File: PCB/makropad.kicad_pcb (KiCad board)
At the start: 2 copper layers, 82 x 85 mm, 55 parts, among them J1 OLED_DISPLAY, J2 Conn_01x04, SW1 SW_Push_45deg, SW10 SW_Push_45deg, SW11 RotaryEncoder_Switch, SW12 RotaryEncoder_Switch, SW2 SW_Push_45deg, SW3 SW_Push_45deg, SW4 SW_Push_45deg, SW5 SW_Push_45deg, SW6 SW_Push_45deg, SW7 SW_Push_45deg, SW8 SW_Push_45deg, SW9 SW_Push_45deg, U1 PCF8574A, U2 MOUDLE-SEEEDUINO-XIAO

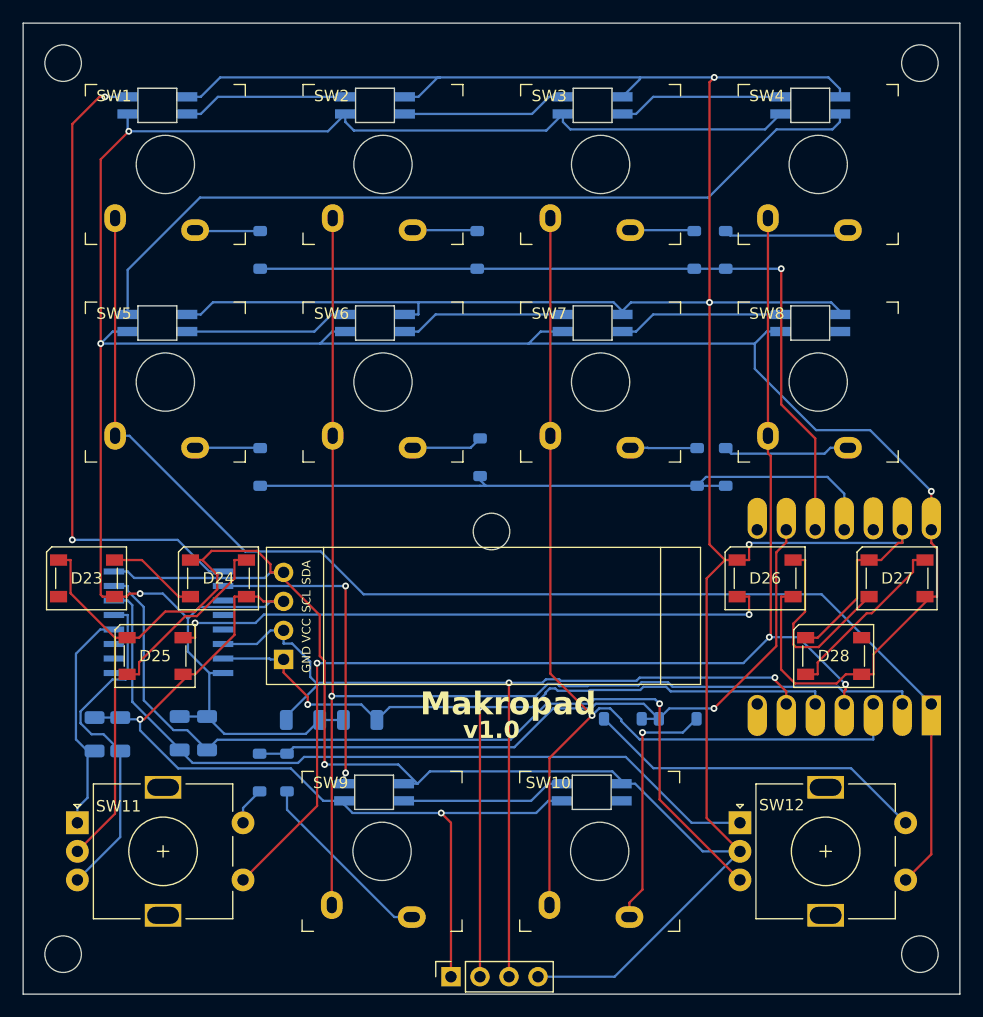
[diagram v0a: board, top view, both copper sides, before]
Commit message: feat: pull up i2c lines to 3.3v and remove encoder pull ups
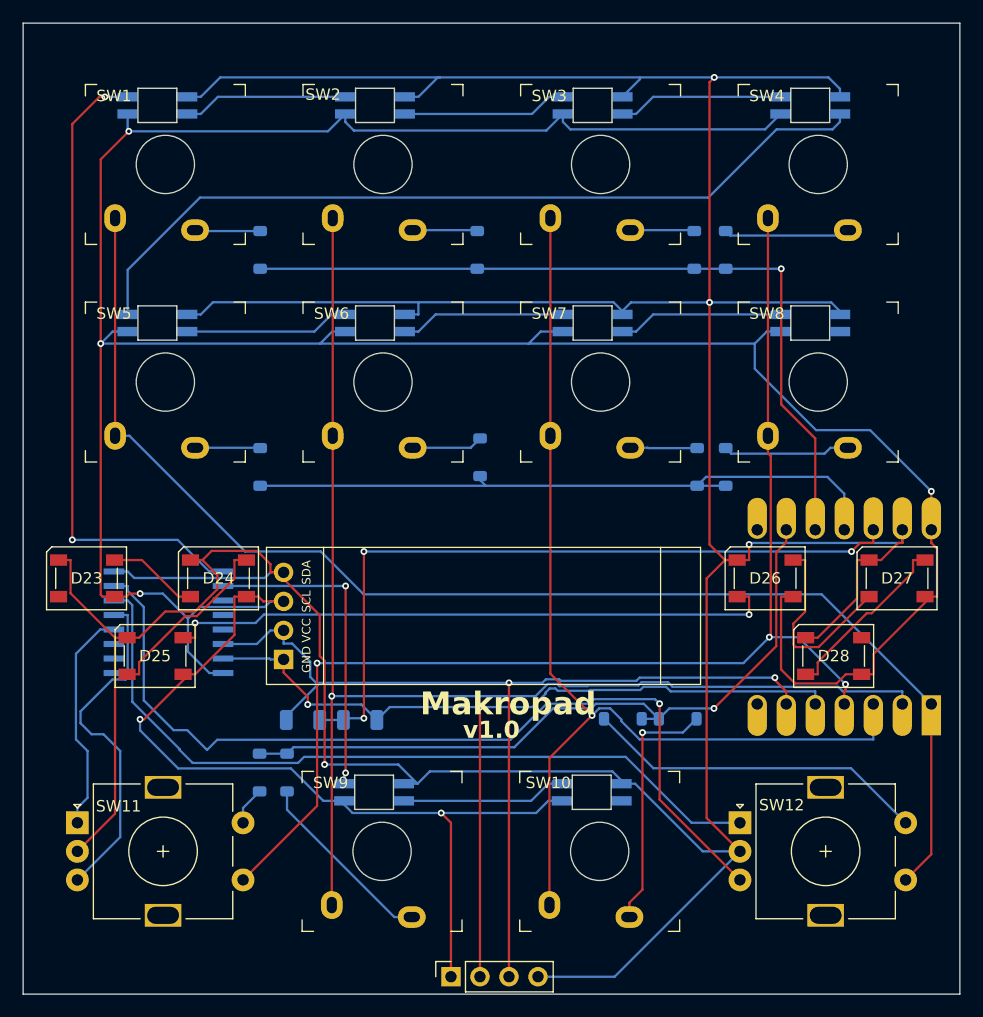
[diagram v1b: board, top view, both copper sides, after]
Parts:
- removed MH1, MH2, MH3, MH4 (x2): MountingHole_3.2mm_M3, MountingHole:MountingHole_3.2mm_M3
- removed R3, R4, R5, R6: 10k, Resistor_SMD:R_1206_3216Metric
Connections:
- R1 pad 2: VCC -> +3.3V
- R2 pad 2: VCC -> +3.3V
- U2 pad 12: unconnected-(U2-3V3-Pad12) -> +3.3V
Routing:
- net +3.3V: track 0.00 -> 64.6 mm, vias 0 -> 3
- net VCC: track 354.4 -> 331.0 mm
- net ENC_1_A: track 20.4 -> 19.8 mm

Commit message: fuck
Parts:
- D13, D14, D15, D16, D17, D18, D19, D20, D21, D22: footprint Components:SK6812MINI-E -> Components:LED_SK6812MINI
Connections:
- U1 pad 11: unconnected-(U1-P6-Pad11) -> STATUS_LED
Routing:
- net VCC: track 331.0 -> 366.6 mm, vias 6 -> 7
- net STATUS_LED: track 0.00 -> 25.4 mm, vias 0 -> 1
- net Net-(D16-DOUT): track 72.3 -> 80.3 mm
- net COL2: track 92.4 -> 99.8 mm
- net COL1: track 112.2 -> 119.6 mm
- net RGB: track 56.6 -> 50.8 mm
- net ROW1: track 58.8 -> 55.3 mm
- net RGB2: track 28.1 -> 31.2 mm
- net GND: track 380.8 -> 379.6 mm
- net Net-(D10-A): track 16.4 -> 17.4 mm
- net COL0: track 116.6 -> 117.2 mm

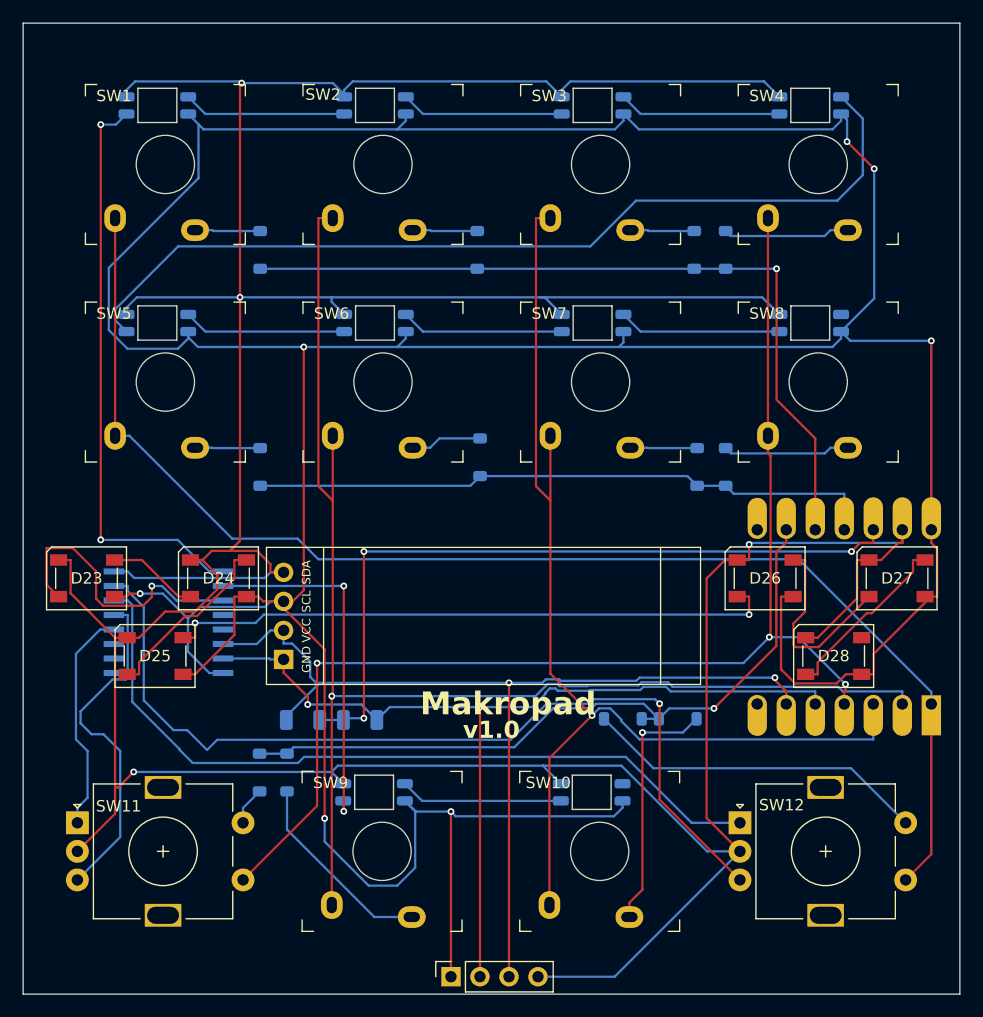
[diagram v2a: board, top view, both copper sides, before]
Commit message: finally finish up pcb and fix led wiring
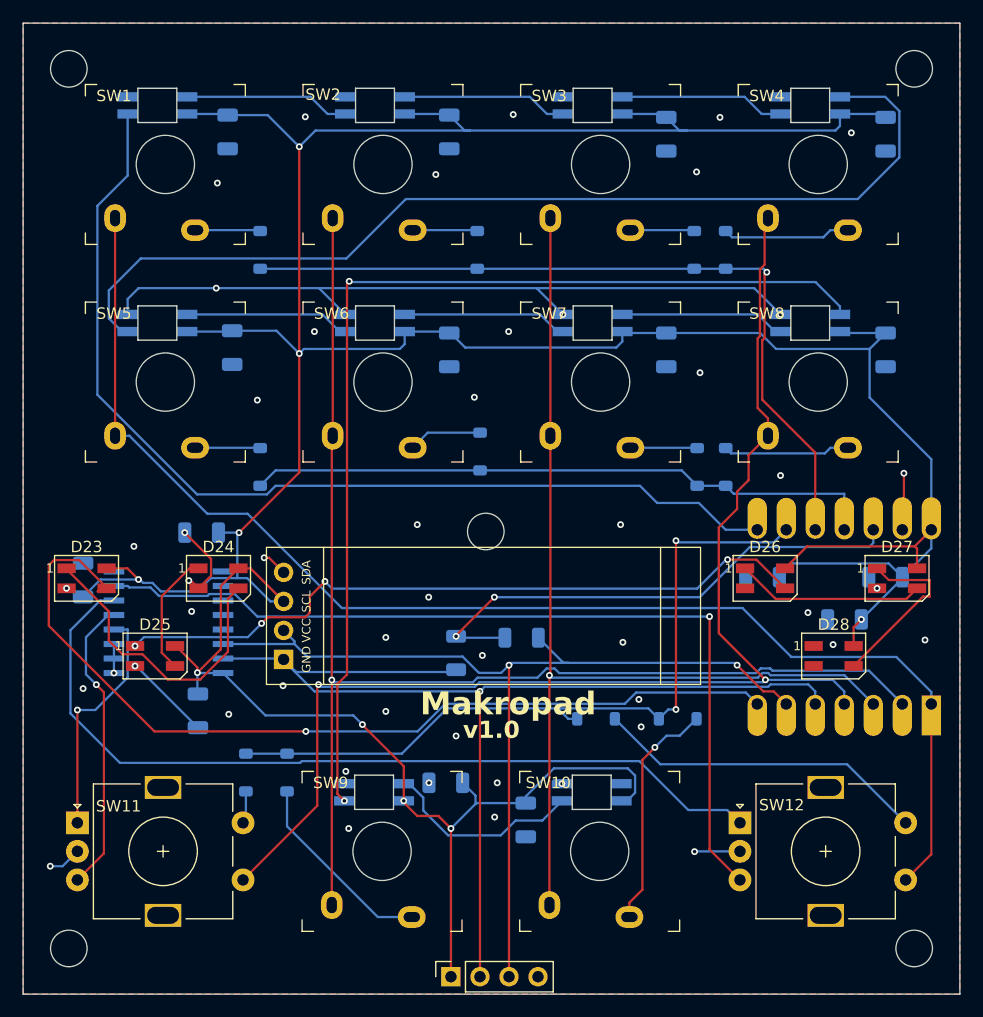
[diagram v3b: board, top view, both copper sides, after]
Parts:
- added C1: 0.1uF, Capacitor_SMD:C_1206_3216Metric, B.Cu at (129.4, 52.5)
- added C10: 0.1uF, Capacitor_SMD:C_1206_3216Metric, B.Cu at (155.5, 112.8)
- added C11: 0.1uF, Capacitor_SMD:C_1206_3216Metric, B.Cu at (116.8, 91.8)
- added C12: 0.1uF, Capacitor_SMD:C_1206_3216Metric, B.Cu at (127.1, 87.6)
- added C13: 0.1uF, Capacitor_SMD:C_1206_3216Metric, B.Cu at (126.8, 103.2)
- added C14: 0.1uF, Capacitor_SMD:C_1206_3216Metric, B.Cu at (176.2, 91.5)
- added C15: 0.1uF, Capacitor_SMD:C_1206_3216Metric, B.Cu at (183.4, 95.2)
- added C16: 0.1uF, Capacitor_SMD:C_1206_3216Metric, B.Cu at (187.0, 91.5)
- added C2: 0.1uF, Capacitor_SMD:C_1206_3216Metric, B.Cu at (148.8, 52.5)
- added C3: 0.1uF, Capacitor_SMD:C_1206_3216Metric, B.Cu at (167.8, 52.7)
- added C4: 0.1uF, Capacitor_SMD:C_1206_3216Metric, B.Cu at (187.0, 52.7)
- added C5: 0.1uF, Capacitor_SMD:C_1206_3216Metric, B.Cu at (129.8, 71.4)
- added C6: 0.1uF, Capacitor_SMD:C_1206_3216Metric, B.Cu at (148.8, 71.6)
- added C7: 0.1uF, Capacitor_SMD:C_1206_3216Metric, B.Cu at (167.8, 71.6)
- added C8: 0.1uF, Capacitor_SMD:C_1206_3216Metric, B.Cu at (187.0, 71.6)
- added C9: 0.1uF, Capacitor_SMD:C_1206_3216Metric, B.Cu at (148.5, 109.5)
- added MH1: MountingHole_3.2mm_M3, MountingHole:MountingHole_3.2mm_M3, F.Cu at (115.5, 47.0)
- added MH2: MountingHole_3.2mm_M3, MountingHole:MountingHole_3.2mm_M3, F.Cu at (189.5, 47.0)
- added MH3: MountingHole_3.2mm_M3, MountingHole:MountingHole_3.2mm_M3, F.Cu at (115.5, 124.0)
- added MH4: MountingHole_3.2mm_M3, MountingHole:MountingHole_3.2mm_M3, F.Cu at (189.5, 124.0)
- added MH5: MountingHole_3.2mm_M3, MountingHole:MountingHole_3.2mm_M3, B.Cu at (152.0, 87.5)
- D13, D14, D15, D16, D17, D18, D19, D20, D21, D22: footprint Components:LED_SK6812MINI -> neopixel.petty:SK6812MINI-E
- D23, D24, D25, D26, D27, D28: footprint LED_SMD:LED_SK6812_PLCC4_5.0x5.0mm_P3.2mm -> LED_SMD:LED_SK6812MINI_PLCC4_3.5x3.5mm_P1.75mm
- moved R2 20.4 mm to (155.1, 96.8), turned to 180 degrees
- moved R1 10.2 mm to (149.4, 98.1), turned to 90 degrees
- moved D9 2.35 mm to (161.7, 103.9), turned to 0 degrees
- moved D12 1.20 mm to (131.0, 108.6)
- moved D6 0.50 mm to (151.5, 80.5)
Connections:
- D13 pad 1: GND -> Net-(D13-DOUT)
- D13 pad 2: RGB -> GND
- D13 pad 3: VCC -> RGB
- D13 pad 4: Net-(D13-DOUT) -> VCC
- D14 pad 1: GND -> Net-(D14-DOUT)
- D14 pad 2: Net-(D13-DOUT) -> GND
- D14 pad 3: VCC -> Net-(D13-DOUT)
- D14 pad 4: Net-(D14-DOUT) -> VCC
- D15 pad 1: GND -> Net-(D15-DOUT)
- D15 pad 2: Net-(D14-DOUT) -> GND
- D15 pad 3: VCC -> Net-(D14-DOUT)
- D15 pad 4: Net-(D15-DOUT) -> VCC
- D16 pad 1: GND -> Net-(D16-DOUT)
- D16 pad 2: Net-(D15-DOUT) -> GND
- D16 pad 3: VCC -> Net-(D15-DOUT)
- D16 pad 4: Net-(D16-DOUT) -> VCC
- D17 pad 1: GND -> Net-(D17-DOUT)
- D17 pad 2: Net-(D16-DOUT) -> GND
- D17 pad 3: VCC -> Net-(D16-DOUT)
- D17 pad 4: Net-(D17-DOUT) -> VCC
- D18 pad 1: GND -> Net-(D18-DOUT)
- D18 pad 2: Net-(D17-DOUT) -> GND
- D18 pad 3: VCC -> Net-(D17-DOUT)
- D18 pad 4: Net-(D18-DOUT) -> VCC
- D19 pad 1: GND -> Net-(D19-DOUT)
- D19 pad 2: Net-(D18-DOUT) -> GND
- D19 pad 3: VCC -> Net-(D18-DOUT)
- D19 pad 4: Net-(D19-DOUT) -> VCC
- D20 pad 1: GND -> Net-(D20-DOUT)
- D20 pad 2: Net-(D19-DOUT) -> GND
- D20 pad 3: VCC -> Net-(D19-DOUT)
- D20 pad 4: unconnected-(D20-DOUT-Pad4) -> VCC
- D21 pad 1: GND -> Net-(D21-DOUT)
- D21 pad 2: RGB2 -> GND
- D21 pad 3: VCC -> Net-(D20-DOUT)
- D21 pad 4: Net-(D21-DOUT) -> VCC
- D22 pad 1: GND -> unconnected-(D22-DOUT-Pad1)
- D22 pad 2: Net-(D21-DOUT) -> GND
- D22 pad 3: VCC -> Net-(D21-DOUT)
- D22 pad 4: unconnected-(D22-DOUT-Pad4) -> VCC
- D23 pad 1: GND -> Net-(D23-DOUT)
- D23 pad 2: STATUS_LED -> GND
- D23 pad 3: VCC -> STATUS_LED
- D23 pad 4: Net-(D23-DOUT) -> VCC
- D24 pad 1: GND -> Net-(D24-DOUT)
- D24 pad 2: Net-(D23-DOUT) -> GND
- D24 pad 3: VCC -> Net-(D23-DOUT)
- D24 pad 4: Net-(D24-DOUT) -> VCC
- D25 pad 1: GND -> Net-(D25-DOUT)
- D25 pad 2: Net-(D24-DOUT) -> GND
- D25 pad 3: VCC -> Net-(D24-DOUT)
- D25 pad 4: Net-(D25-DOUT) -> VCC
- D26 pad 1: GND -> Net-(D26-DOUT)
- D26 pad 2: Net-(D25-DOUT) -> GND
- D26 pad 3: VCC -> Net-(D25-DOUT)
- D26 pad 4: Net-(D26-DOUT) -> VCC
- D27 pad 1: GND -> Net-(D27-DOUT)
- D27 pad 2: Net-(D26-DOUT) -> GND
- D27 pad 3: VCC -> Net-(D26-DOUT)
- D27 pad 4: Net-(D27-DOUT) -> VCC
- D28 pad 1: GND -> unconnected-(D28-DOUT-Pad1)
- D28 pad 2: Net-(D27-DOUT) -> GND
- D28 pad 3: VCC -> Net-(D27-DOUT)
- D28 pad 4: unconnected-(D28-DOUT-Pad4) -> VCC
- U1 pad 1: unconnected-(U1-A0-Pad1) -> GND
- U1 pad 10: RGB2 -> unconnected-(U1-P5-Pad10)
- U1 pad 11: STATUS_LED -> unconnected-(U1-P6-Pad11)
- U1 pad 2: unconnected-(U1-A1-Pad2) -> GND
- U1 pad 3: unconnected-(U1-A2-Pad3) -> GND
- U1 pad 9: RGB -> unconnected-(U1-P4-Pad9)
- U2 pad 7: unconnected-(U2-PB08_A6_D6_TX-Pad7) -> STATUS_LED
- U2 pad 8: unconnected-(U2-PB09_A7_D7_RX-Pad8) -> RGB
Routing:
- net GND: track 379.6 -> 99.5 mm, vias 4 -> 50
- net Net-(D20-DOUT): track 0.00 -> 90.7 mm, vias 0 -> 2
- net STATUS_LED: track 25.4 -> 80.2 mm
- net RGB: track 50.8 -> 89.0 mm, vias 2 -> 0
- net RGB2: track 31.2 -> 0.00 mm, vias 2 -> 0
- net +3.3V: track 64.6 -> 45.4 mm, vias 3 -> 2
- net Net-(D23-DOUT): track 7.98 -> 26.6 mm
- net I2C_SDA: track 81.6 -> 96.0 mm, vias 2 -> 1
- net COL2: track 99.8 -> 89.9 mm
- net Net-(D25-DOUT): track 53.8 -> 62.4 mm, vias 2 -> 4
- net Net-(D16-DOUT): track 80.3 -> 88.4 mm
- net VCC: track 366.6 -> 358.9 mm, vias 7 -> 9
- net COL1: track 119.6 -> 112.3 mm
- net ENC_2_A: track 68.3 -> 74.9 mm
- net Net-(D24-DOUT): track 16.2 -> 10.8 mm
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- added copper zone on B.Cu, net GND
- added copper zone on F.Cu, net GND

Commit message: fix some stuff + firmware
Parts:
- moved D12 42.5 mm to (173.5, 108.2)
- moved D9 31.0 mm to (131.0, 108.5), turned to -90 degrees
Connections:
- D12 pad 2: ENC_1_SWA -> ENC_2_SWA
- D9 pad 2: ENC_2_SWA -> ENC_1_SWA
- SW11 pad S1: COL3 -> COL0
- SW12 pad S1: COL0 -> COL3
- U2 pad 10: ROW0 -> ROW1
- U2 pad 11: ROW1 -> ROW0
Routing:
- net COL3: track 112.4 -> 71.8 mm, vias 2 -> 1
- net COL0: track 117.2 -> 130.6 mm, vias 0 -> 3
- net ENC_2_SWA: track 29.2 -> 16.5 mm
- net ROW2: track 67.0 -> 72.0 mm
- net ROW1: track 55.7 -> 51.9 mm
- net STATUS_LED: track 80.2 -> 78.5 mm
- net ROW0: track 69.1 -> 70.7 mm
- net VCC: track 358.9 -> 357.8 mm
